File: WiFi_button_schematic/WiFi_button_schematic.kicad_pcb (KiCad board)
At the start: 2 copper layers, 22 x 79 mm, 15 parts, among them J1 Conn_01x05_Male, SW1 SW_Push, U1 HT75xx-1-SOT89, U2 ESP-12E, U3 TC4056A_module

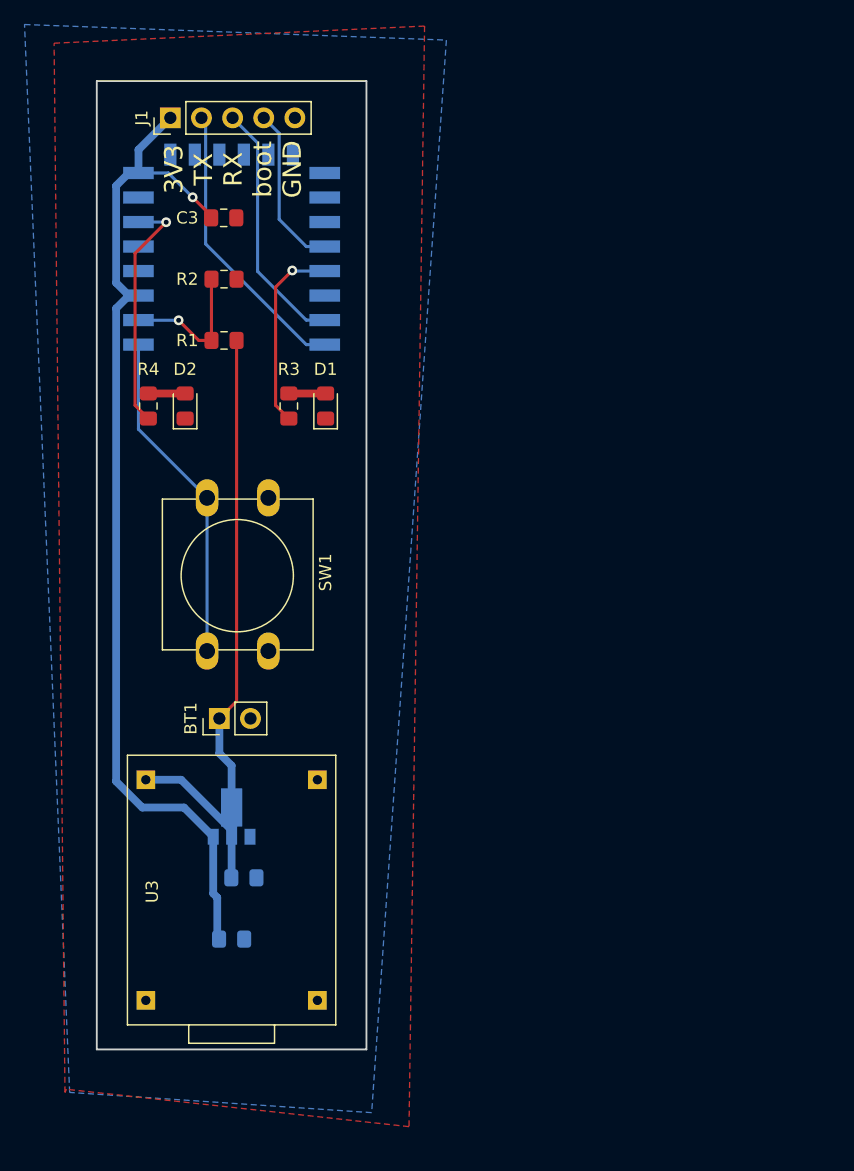
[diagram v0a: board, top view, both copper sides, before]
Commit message: Changed capacitors' and resistors' sizes to 1206
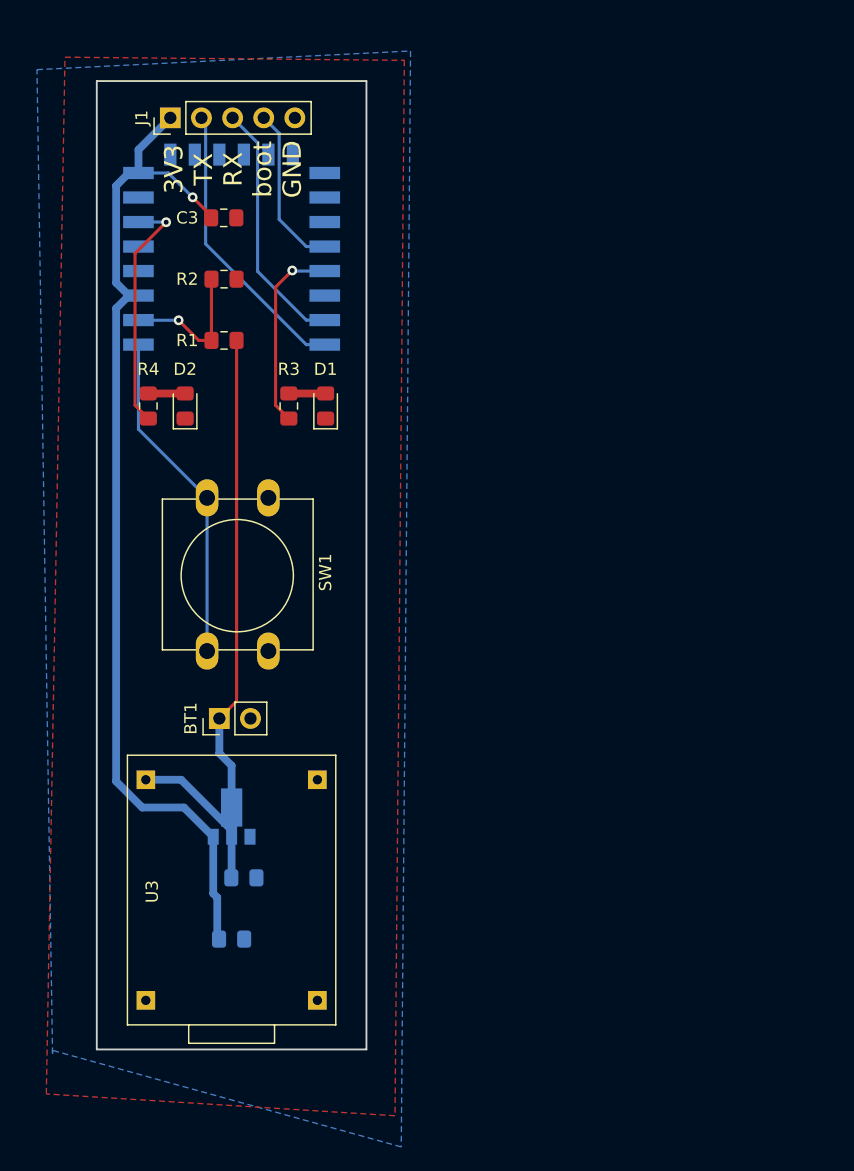
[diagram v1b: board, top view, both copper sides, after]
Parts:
- C3: value 0.1uF -> 100nF
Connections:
- net /~RST renamed /Btn
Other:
- board text added: "v02"
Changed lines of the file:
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@@
   (general
     (thickness 1.6)
-    (drawings 5)
+    (drawings 6)
     (tracks 66)
     (zones 0)
@@
   )
   (page A4)
+  (title_block
+    (title web_button)
+    (date 2021-10-04)
+    (rev v02)
+  )
   (layers
     (0 F.Cu signal)
@@
     (47 F.CrtYd user)
     (48 B.Fab user)
-    (49 F.Fab user)
+    (49 F.Fab user hide)
   )
   (setup
@@
       (usegerberextensions true)
       (usegerberattributes false)
-      (usegerberadvancedattributes true)
+      (usegerberadvancedattributes false)
       (creategerberjobfile false)
       (excludeedgelayer true)
@@
   (net 10 /rLed)
   (net 11 /bLed)
-  (net 12 /~RST)
-  (net 13 "Net-(U2-Pad20)")
-  (net 14 "Net-(U2-Pad17)")
-  (net 15 "Net-(U2-Pad16)")
-  (net 16 "Net-(U2-Pad14)")
-  (net 17 "Net-(U2-Pad13)")
-  (net 18 "Net-(U2-Pad12)")
-  (net 19 "Net-(U2-Pad11)")
-  (net 20 "Net-(U2-Pad10)")
-  (net 21 "Net-(U2-Pad9)")
-  (net 22 "Net-(U2-Pad7)")
-  (net 23 "Net-(U2-Pad5)")
-  (net 24 "Net-(U2-Pad4)")
-  (net 25 "Net-(U3-Pad1)")
+  (net 12 "Net-(U2-Pad20)")
+  (net 13 "Net-(U2-Pad17)")
+  (net 14 "Net-(U2-Pad16)")
+  (net 15 "Net-(U2-Pad14)")
+  (net 16 "Net-(U2-Pad13)")
+  (net 17 "Net-(U2-Pad12)")
+  (net 18 "Net-(U2-Pad11)")
+  (net 19 "Net-(U2-Pad10)")
+  (net 20 "Net-(U2-Pad9)")
+  (net 21 "Net-(U2-Pad7)")
+  (net 22 "Net-(U2-Pad5)")
+  (net 23 "Net-(U2-Pad4)")
+  (net 24 "Net-(U3-Pad1)")
+  (net 25 /Btn)
   (net_class Default "This is the default net class."
     (clearance 0.254)
@@
     (add_net +BATT)
     (add_net /BAT_VOL)
+    (add_net /Btn)
     (add_net /RX)
     (add_net /TX)
@@
     (add_net /boot_sel)
     (add_net /rLed)
-    (add_net /~RST)
     (add_net GND)
     (add_net "Net-(D1-Pad2)")
@@
       (net 2 +BATT))
     (pad 1 thru_hole rect (at -9 -7 90) (size 1.524 1.524) (drill 0.762) (layers *.Cu *.Mask)
-      (net 25 "Net-(U3-Pad1)"))
+      (net 24 "Net-(U3-Pad1)"))
     (pad 2 thru_hole rect (at -9 7 90) (size 1.524 1.524) (drill 0.762) (layers *.Cu *.Mask Eco2.User)
       (net 1 GND))
@@
       (net 7 /RX))
     (pad 20 smd rect (at 7.6 -0.5) (size 2.5 1) (layers B.Cu B.Paste B.Mask)
-      (net 13 "Net-(U2-Pad20)"))
+      (net 12 "Net-(U2-Pad20)"))
     (pad 19 smd rect (at 7.6 -2.5) (size 2.5 1) (layers B.Cu B.Paste B.Mask)
       (net 10 /rLed))
@@
       (net 6 /boot_sel))
     (pad 17 smd rect (at 7.6 -6.5) (size 2.5 1) (layers B.Cu B.Paste B.Mask)
-      (net 14 "Net-(U2-Pad17)"))
+      (net 13 "Net-(U2-Pad17)"))
     (pad 16 smd rect (at 7.6 -8.5) (size 2.5 1) (layers B.Cu B.Paste B.Mask)
-      (net 15 "Net-(U2-Pad16)"))
+      (net 14 "Net-(U2-Pad16)"))
     (pad 15 smd rect (at 7.6 -10.5) (size 2.5 1) (layers B.Cu B.Paste B.Mask)
       (net 1 GND))
     (pad 14 smd rect (at 5 -12) (size 1 1.8) (layers B.Cu B.Paste B.Mask)
-      (net 16 "Net-(U2-Pad14)"))
+      (net 15 "Net-(U2-Pad14)"))
     (pad 13 smd rect (at 3 -12) (size 1 1.8) (layers B.Cu B.Paste B.Mask)
-      (net 17 "Net-(U2-Pad13)"))
+      (net 16 "Net-(U2-Pad13)"))
     (pad 12 smd rect (at 1 -12) (size 1 1.8) (layers B.Cu B.Paste B.Mask)
-      (net 18 "Net-(U2-Pad12)"))
+      (net 17 "Net-(U2-Pad12)"))
     (pad 11 smd rect (at -1 -12) (size 1 1.8) (layers B.Cu B.Paste B.Mask)
-      (net 19 "Net-(U2-Pad11)"))
+      (net 18 "Net-(U2-Pad11)"))
     (pad 10 smd rect (at -3 -12) (size 1 1.8) (layers B.Cu B.Paste B.Mask)
-      (net 20 "Net-(U2-Pad10)"))
+      (net 19 "Net-(U2-Pad10)"))
     (pad 9 smd rect (at -5 -12) (size 1 1.8) (layers B.Cu B.Paste B.Mask)
-      (net 21 "Net-(U2-Pad9)"))
+      (net 20 "Net-(U2-Pad9)"))
     (pad 8 smd rect (at -7.6 -10.5) (size 2.5 1) (layers B.Cu B.Paste B.Mask)
       (net 3 +3V3))
     (pad 7 smd rect (at -7.6 -8.5) (size 2.5 1) (layers B.Cu B.Paste B.Mask)
-      (net 22 "Net-(U2-Pad7)"))
+      (net 21 "Net-(U2-Pad7)"))
     (pad 6 smd rect (at -7.6 -6.5) (size 2.5 1) (layers B.Cu B.Paste B.Mask)
       (net 11 /bLed))
     (pad 5 smd rect (at -7.6 -4.5) (size 2.5 1) (layers B.Cu B.Paste B.Mask)
-      (net 23 "Net-(U2-Pad5)"))
+      (net 22 "Net-(U2-Pad5)"))
     (pad 4 smd rect (at -7.6 -2.5) (size 2.5 1) (layers B.Cu B.Paste B.Mask)
-      (net 24 "Net-(U2-Pad4)"))
+      (net 23 "Net-(U2-Pad4)"))
     (pad 3 smd rect (at -7.6 -0.5) (size 2.5 1) (layers B.Cu B.Paste B.Mask)
       (net 3 +3V3))
@@
       (net 9 /BAT_VOL))
     (pad 1 smd rect (at -7.6 3.5) (size 2.5 1) (layers B.Cu B.Paste B.Mask)
-      (net 12 /~RST))
+      (net 25 /Btn))
     (model ${KISYS3DMOD}/RF_Module.3dshapes/ESP-12E.wrl
       (at (xyz 0 0 0))
@@
     )
     (pad 2 thru_hole oval (at 0 5 270) (size 3.048 1.85) (drill 1.3) (layers *.Cu *.Mask)
-      (net 12 /~RST))
+      (net 25 /Btn))
     (pad 1 thru_hole oval (at 0 0 270) (size 3.048 1.85) (drill 1.3) (layers *.Cu *.Mask)
       (net 1 GND))
     (pad 2 thru_hole oval (at 12.5 5 270) (size 3.048 1.85) (drill 1.3) (layers *.Cu *.Mask)
-      (net 12 /~RST))
+      (net 25 /Btn))
     (pad 1 thru_hole oval (at 12.5 0 270) (size 3.048 1.85) (drill 1.3) (layers *.Cu *.Mask)
       (net 1 GND))
@@
       (effects (font (size 1 1) (thickness 0.15)))
     )
-    (fp_text value 0.1uF (at 4.025 0) (layer F.Fab)
+    (fp_text value 100nF (at 4.025 0) (layer F.Fab)
       (effects (font (size 1 1) (thickness 0.15)))
     )
@@
       (rotate (xyz 0 0 0))
     )
+  )
+  (gr_text v02 (at 91.44 77.216) (layer B.SilkS)
+    (effects (font (size 1.5 1.5) (thickness 0.3)))
   )
   (gr_text "3V3\nTX\nRX\nboot\nGND" (at 87.122 44.196 90) (layer F.SilkS)
@@
   (segment (start 79.12399 51.05101) (end 79.12399 63.45199) (width 0.254) (layer F.Cu) (net 11))
   (segment (start 81.661 48.514) (end 79.12399 51.05101) (width 0.254) (layer F.Cu) (net 11))
-  (segment (start 79.4 65.4) (end 85 71) (width 0.254) (layer B.Cu) (net 12))
-  (segment (start 79.4 58.5) (end 79.4 65.4) (width 0.254) (layer B.Cu) (net 12))
-  (segment (start 85 71) (end 85 83.5) (width 0.254) (layer B.Cu) (net 12))
+  (segment (start 79.4 65.4) (end 85 71) (width 0.254) (layer B.Cu) (net 25))
+  (segment (start 79.4 58.5) (end 79.4 65.4) (width 0.254) (layer B.Cu) (net 25))
+  (segment (start 85 71) (end 85 83.5) (width 0.254) (layer B.Cu) (net 25))
   (zone (net 1) (net_name GND) (layer F.Cu) (hatch edge 0.508)
     (connect_pads (clearance 0.508))
@@
     (polygon
       (pts
-        (xy 101.473 122.301) (xy 73.533 119.253) (xy 73.406 119.507) (xy 72.517 33.909) (xy 102.743 32.512)
+        (xy 101.092 35.306) (xy 100.33 121.412) (xy 71.882 119.634) (xy 73.406 35.052)
       )
     )
@@
     (polygon
       (pts
-        (xy 104.521 33.655) (xy 98.425 121.158) (xy 73.787 119.507) (xy 70.104 32.385)
+        (xy 100.838 123.952) (xy 72.39 116.078) (xy 72.39 116.332) (xy 71.12 36.068) (xy 101.6 34.544)
       )
     )

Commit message: Project is now less complicated
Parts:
- removed BT1: 3.7V, Connector_PinHeader_2.54mm:PinHeader_1x02_P2.54mm_Vertical
- removed C1, C2: 10uF, Capacitor_SMD:C_0805_2012Metric_Pad1.15x1.40mm_HandSolder
- removed C3: 100nF, Capacitor_SMD:C_0805_2012Metric_Pad1.15x1.40mm_HandSolder
- removed D1: Red, LED_SMD:LED_0805_2012Metric_Pad1.15x1.40mm_HandSolder
- removed D2: Blue, LED_SMD:LED_0805_2012Metric_Pad1.15x1.40mm_HandSolder
- removed J1: Conn_01x05_Male, Connector_PinHeader_2.54mm:PinHeader_1x05_P2.54mm_Vertical
- removed R1: 47K, Resistor_SMD:R_0805_2012Metric_Pad1.15x1.40mm_HandSolder
- removed R2: 10K, Resistor_SMD:R_0805_2012Metric_Pad1.15x1.40mm_HandSolder
- removed R3, R4: 1K, Resistor_SMD:R_0805_2012Metric_Pad1.15x1.40mm_HandSolder
- removed SW1: SW_Push, Button_Switch_THT:SW_PUSH-12mm
- removed U1: HT75xx-1-SOT89, Package_TO_SOT_SMD:SOT-89-3
- removed U2: ESP-12E, RF_Module:ESP-12E
- removed U3: TC4056A_module, WiFi_button:TC4056_module
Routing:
- net +3V3: track 83.9 -> 0.00 mm, vias 1 -> 0
- net +BATT: track 54.0 -> 0.00 mm
- net /Btn: track 27.3 -> 0.00 mm
- net /TX: track 23.5 -> 0.00 mm
- net /RX: track 20.5 -> 0.00 mm
- net /bLed: track 19.8 -> 0.00 mm, vias 1 -> 0
- net /rLed: track 15.8 -> 0.00 mm, vias 1 -> 0
- net /boot_sel: track 13.4 -> 0.00 mm
- net /BAT_VOL: track 11.6 -> 0.00 mm, vias 1 -> 0
- net Net-(D2-Pad2): track 3.00 -> 0.00 mm
- net Net-(D1-Pad2): track 3.00 -> 0.00 mm
- removed copper zone on B.Cu, net GND
- removed copper zone on F.Cu, net GND
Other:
- board outline removed
- board text removed: "3V3 TX RX boot GND"
- board text removed: "v02"

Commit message: V02 of schematic finished
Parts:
- added BT1: 3.7V, Connector_PinHeader_2.54mm:PinHeader_1x02_P2.54mm_Vertical, F.Cu at (82.0, 42.8)
- added C1: 10uF, Capacitor_SMD:C_1206_3216Metric_Pad1.33x1.80mm_HandSolder, F.Cu at (81.5, 56.0)
- added C2: 10uF, Capacitor_SMD:C_1206_3216Metric_Pad1.33x1.80mm_HandSolder, F.Cu at (87.0, 51.0)
- added C3: 100nF, Capacitor_SMD:C_1206_3216Metric_Pad1.33x1.80mm_HandSolder, F.Cu at (92.0, 51.0)
- added D1: Red, LED_SMD:LED_1206_3216Metric_Pad1.42x1.75mm_HandSolder, F.Cu at (82.8, 64.8)
- added D2: Green, LED_SMD:LED_1206_3216Metric_Pad1.42x1.75mm_HandSolder, F.Cu at (86.5, 64.8)
- added D3: Green, LED_SMD:LED_1206_3216Metric_Pad1.42x1.75mm_HandSolder, F.Cu at (90.2, 64.8)
- added J1: Conn_01x06_Female, Connector_PinHeader_2.54mm:PinHeader_1x06_P2.54mm_Vertical, F.Cu at (130.0, 55.4)
- added Q1: MMBT3904, Package_TO_SOT_SMD:SOT-23_Handsoldering, B.Cu at (125.0, 53.8)
- added Q2: MMBT3904, Package_TO_SOT_SMD:SOT-23_Handsoldering, B.Cu at (124.8, 44.2)
- added R1: 10K, Resistor_SMD:R_1206_3216Metric_Pad1.30x1.75mm_HandSolder, F.Cu at (120.2, 54.0)
- added R2: 1K, Resistor_SMD:R_1206_3216Metric_Pad1.30x1.75mm_HandSolder, B.Cu at (82.8, 64.8)
- added R3: 10K, Resistor_SMD:R_1206_3216Metric_Pad1.30x1.75mm_HandSolder, F.Cu at (120.0, 44.7)
- added R4: 1K, Resistor_SMD:R_1206_3216Metric_Pad1.30x1.75mm_HandSolder, B.Cu at (86.5, 64.8)
- added R5: 1K, Resistor_SMD:R_1206_3216Metric_Pad1.30x1.75mm_HandSolder, B.Cu at (90.2, 64.8)
- added R8: 10K, Resistor_SMD:R_1206_3216Metric_Pad1.30x1.75mm_HandSolder, B.Cu at (96.2, 64.8)
- added R9: 10K, Resistor_SMD:R_1206_3216Metric_Pad1.30x1.75mm_HandSolder, F.Cu at (117.0, 55.5)
- added SW1: SW_Push, custom_buttons_switches:sw_push_12_x_12_mm, F.Cu at (102.5, 66.5)
- added U1: HT75xx-1-SOT89, Package_TO_SOT_SMD:SOT-89-3_Handsoldering, F.Cu at (82.0, 50.5)
- added U2: ESP-12E, RF_Module:ESP-12E, F.Cu at (105.2, 45.5)
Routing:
- net +3V3: track 0.00 -> 84.7 mm, vias 0 -> 1
- net /~RST: track 0.00 -> 60.0 mm, vias 0 -> 3
- net /rLed: track 0.00 -> 40.9 mm, vias 0 -> 3
- net /bLed: track 0.00 -> 37.3 mm, vias 0 -> 3
- net /TX: track 0.00 -> 19.0 mm
- net /RX: track 0.00 -> 18.7 mm
- net /CTS: track 0.00 -> 16.9 mm, vias 0 -> 1
- net /gLed: track 0.00 -> 15.8 mm, vias 0 -> 1
- net /DTR: track 0.00 -> 15.3 mm, vias 0 -> 1
- net +BATT: track 0.00 -> 13.7 mm
- net /boot_sel: track 0.00 -> 12.8 mm, vias 0 -> 1
- net Net-(Q1-Pad1): track 0.00 -> 8.43 mm, vias 0 -> 1
- net Net-(Q2-Pad1): track 0.00 -> 6.31 mm, vias 0 -> 1
- net Net-(R9-Pad1): track 0.00 -> 4.17 mm
- net Net-(D3-Pad2): track 0.00 -> 2.96 mm, vias 0 -> 1
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- added copper zone on B.Cu, net GND
- added copper zone on F.Cu, net GND
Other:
- board outline added: 53.4 x 32.9 mm
- net class Default: clearance 0.254 -> 0.127; trace_width 0.254 -> 0.127; via_dia 0.8 -> 0.6; via_drill 0.4 -> 0.3
- rule pad_to_mask_clearance: 0.05 -> 0
- rule trace_clearance: 0.254 -> 0.127
- rule trace_min: 0.2 -> 0.127
- rule via_min_size: 0.4 -> 0.6
- board text added: "+"
- board text added: "-"
- board text added: "3V3"
- board text added: "CTS"
- board text added: "DTR"
- board text added: "GND"
- board text added: "RX"
- board text added: "TX"
- board text added: "V02"
- board text added: "WiFi button by MKrysz"

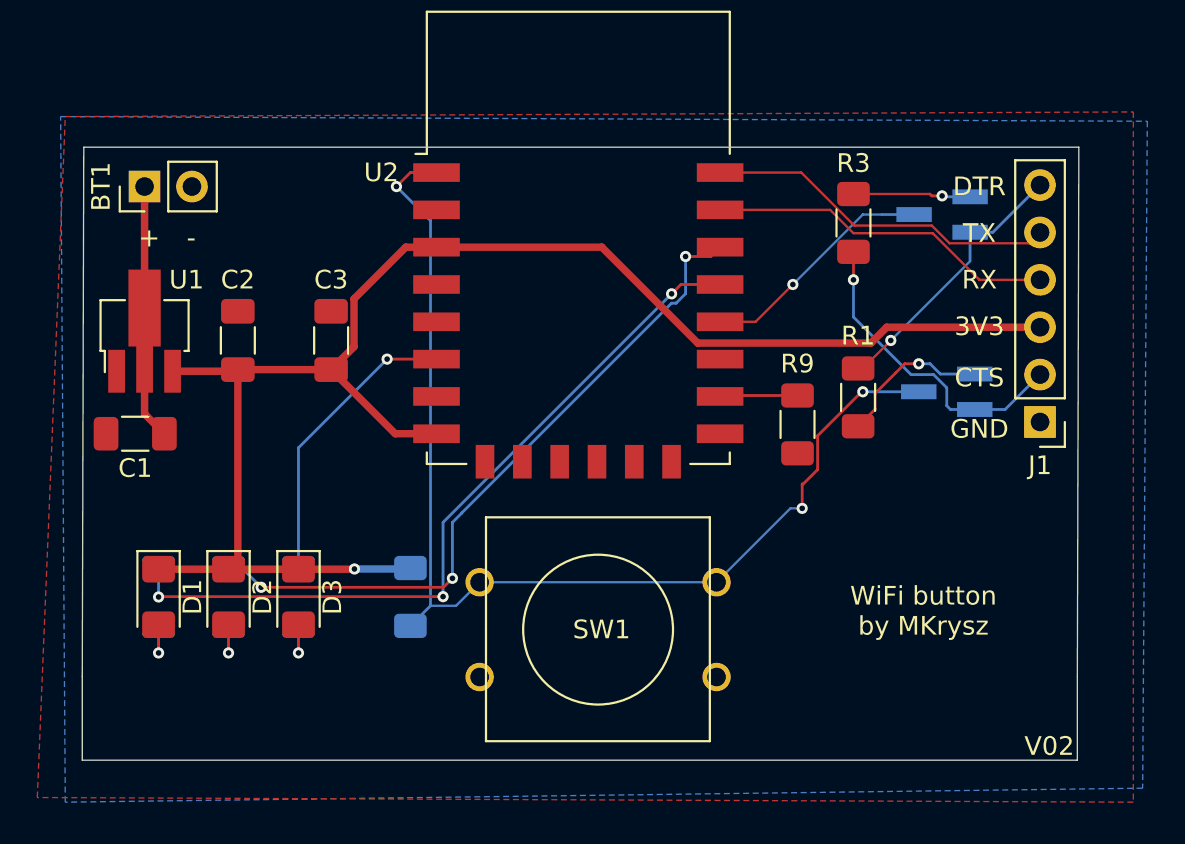
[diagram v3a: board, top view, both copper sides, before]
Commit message: Added circuit for measuring battery voltage
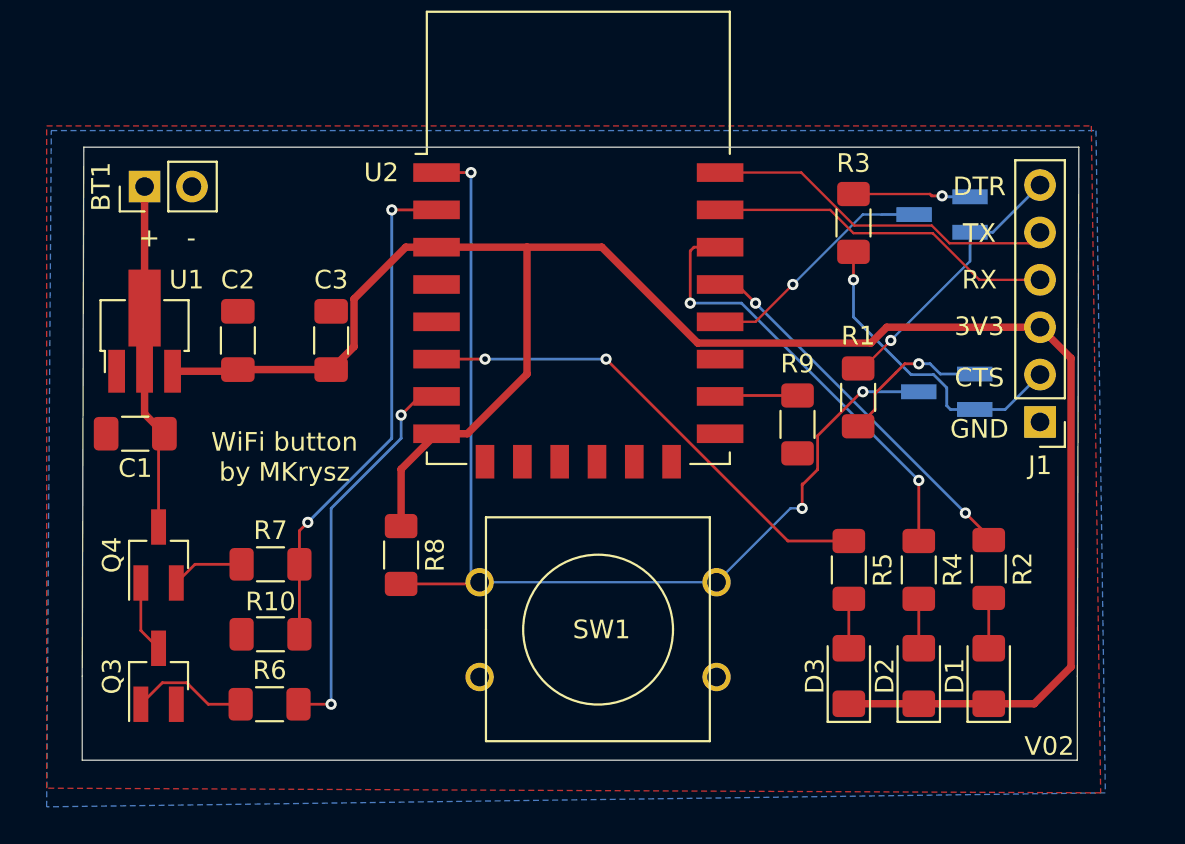
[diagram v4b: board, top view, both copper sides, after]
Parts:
- added Q3: MMBT3904, Package_TO_SOT_SMD:SOT-23_Handsoldering, F.Cu at (82.8, 69.0)
- added Q4: MMBT3906, Package_TO_SOT_SMD:SOT-23_Handsoldering, F.Cu at (82.8, 62.5)
- added R10: 10K, Resistor_SMD:R_1206_3216Metric_Pad1.30x1.75mm_HandSolder, F.Cu at (88.8, 66.8)
- added R6: 47K, Resistor_SMD:R_1206_3216Metric_Pad1.30x1.75mm_HandSolder, F.Cu at (88.7, 70.5)
- added R7: 47K, Resistor_SMD:R_1206_3216Metric_Pad1.30x1.75mm_HandSolder, F.Cu at (88.8, 63.0)
- R2, R4, R5, R8: moved to F.Cu
- moved D1 44.7 mm to (127.2, 69.0), turned to 90 degrees
- moved R2 44.5 mm to (127.2, 63.2)
- moved D2 37.2 mm to (123.5, 69.0), turned to 90 degrees
- moved R4 37.0 mm to (123.5, 63.3)
- moved D3 29.8 mm to (119.8, 69.0), turned to 90 degrees
- moved R5 29.5 mm to (119.8, 63.3)
- moved R8 2.30 mm to (95.8, 62.5)
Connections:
- U2 pad 2: (no net) -> /ADC_IN
- U2 pad 7: (no net) -> /ADC_EN
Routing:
- net /ADC_IN: track 0.00 -> 27.2 mm, vias 0 -> 2
- net /ADC_EN: track 0.00 -> 21.1 mm, vias 0 -> 2
- net /rLed: track 40.9 -> 20.2 mm, vias 3 -> 2
- net +3V3: track 84.7 -> 103.6 mm, vias 1 -> 0
- net /bLed: track 37.3 -> 23.9 mm, vias 3 -> 2
- net /gLed: track 15.8 -> 26.1 mm, vias 1 -> 2
- net Net-(Q3-Pad1): track 0.00 -> 6.30 mm
- net +BATT: track 13.7 -> 18.8 mm
- net Net-(Q4-Pad2): track 0.00 -> 3.91 mm
- net Net-(Q3-Pad3): track 0.00 -> 3.89 mm
- net /~RST: track 60.0 -> 58.5 mm
- net Net-(D3-Pad2): track 2.96 -> 2.65 mm, vias 1 -> 0
- net Net-(D2-Pad2): track 2.96 -> 2.65 mm, vias 1 -> 0
- net Net-(D1-Pad2): track 2.96 -> 2.70 mm, vias 1 -> 0

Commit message: Version v02
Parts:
- moved Q4 0.50 mm to (82.7, 62.0), turned to 270 degrees
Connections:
- Q4 pad 2: Net-(Q4-Pad2) -> +BATT
- Q4 pad 3: +BATT -> Net-(Q4-Pad3)
- R7 pad 1: Net-(Q4-Pad2) -> Net-(Q4-Pad3)
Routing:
- net Net-(Q4-Pad3): track 0.00 -> 4.71 mm
- net Net-(Q3-Pad3): track 3.89 -> 7.91 mm
- net Net-(Q4-Pad2): track 3.91 -> 0.00 mm
